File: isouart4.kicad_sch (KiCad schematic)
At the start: 25 parts, among them J1 USB_B, J2 Conn_01x04, J3 Conn_01x04, J4 Conn_01x04, J5 Conn_01x04, U1 AMS1117-3.3, U2 π122U31, U3 π122U31, U4 π122U31, U5 π122U31

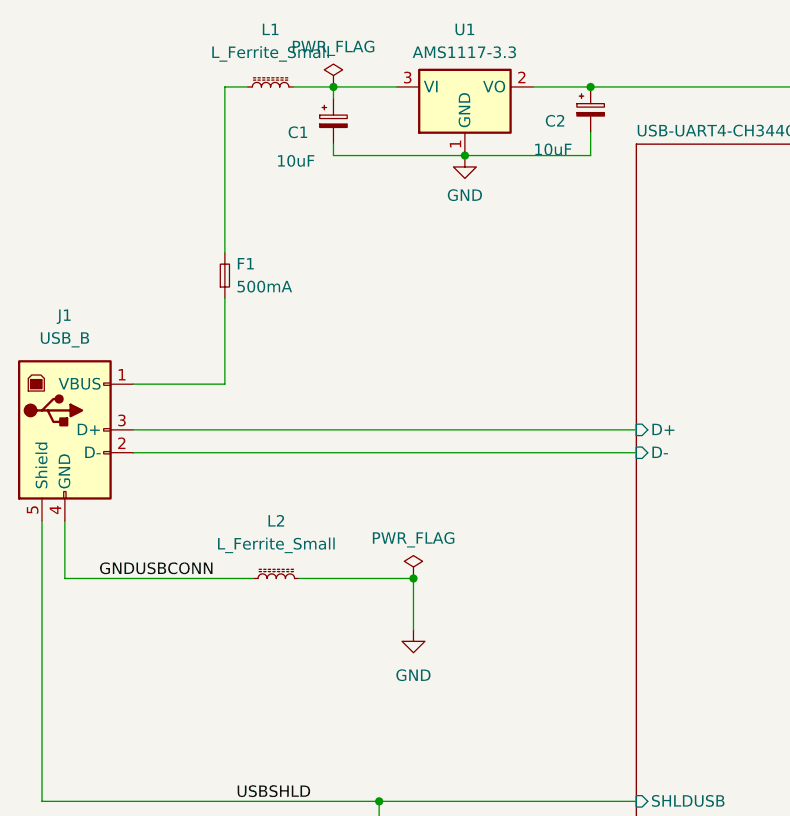
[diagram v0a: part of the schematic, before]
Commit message: adjust power filtering
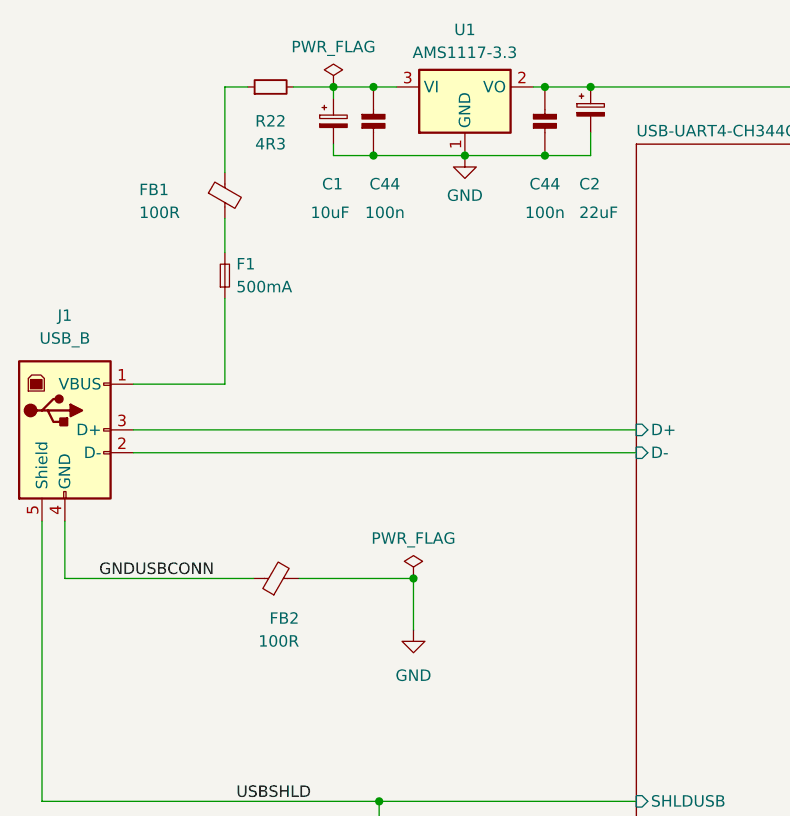
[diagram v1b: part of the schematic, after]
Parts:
- removed L1, L2: L_Ferrite_Small, isouart4:FB_0805_2012Metric, symbol isouart4:L_Ferrite_Small
- added C44 (x2): 100n, Capacitor_SMD:C_0805_2012Metric_Pad1.18x1.45mm_HandSolder, symbol isouart4:CAP_NP
- added FB1, FB2: 100R, isouart4:FB_0805_2012Metric, symbol Device:FerriteBead_Small
- added R22: 4R3, Resistor_SMD:R_2512_6332Metric_Pad1.40x3.35mm_HandSolder, symbol Device:R_Small
- C1: footprint Capacitor_SMD:C_0805_2012Metric_Pad1.18x1.45mm_HandSolder -> Capacitor_Tantalum_SMD:CP_EIA-3528-15_AVX-H_Pad1.50x2.35mm_HandSolder
- C2: value 10uF -> 22uF; footprint Capacitor_SMD:C_0805_2012Metric_Pad1.18x1.45mm_HandSolder -> Capacitor_Tantalum_SMD:CP_EIA-3528-15_AVX-H_Pad1.50x2.35mm_HandSolder
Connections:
- net GND: now also C44.2, C44.2, FB2.2
- net GNDUSBCONN: now also FB2.1
- net USB-UART4-CH344Q/VIN 3.3V: now also C44.1
- net at C1.1, U1.3 (VI): now also C44.1, R22.2
- net at F1.2: now also FB1.2
- new net: FB1.1, R22.1

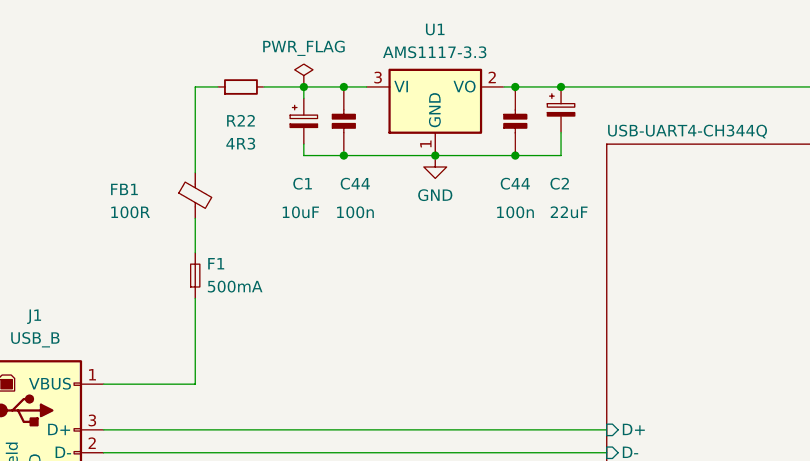
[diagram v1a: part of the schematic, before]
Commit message: AMS1117-3.3 -> LP2950CDT-3.3 (reduce usb downstream capacitance)
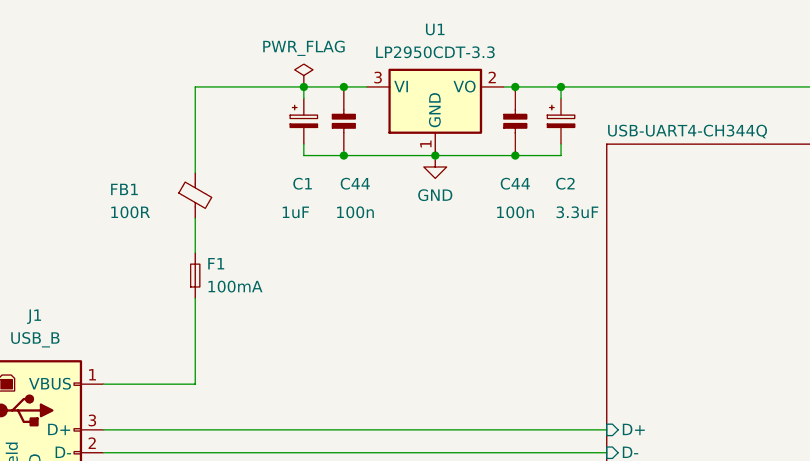
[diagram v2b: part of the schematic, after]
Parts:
- removed R22: 4R3, Resistor_SMD:R_2512_6332Metric_Pad1.40x3.35mm_HandSolder, symbol Device:R_Small
- C1: value 10uF -> 1uF
- C2: value 22uF -> 3.3uF
- F1: value 500mA -> 100mA
- U1: value AMS1117-3.3 -> LP2950CDT-3.3; footprint Package_TO_SOT_SMD:SOT-223-3_TabPin2 -> Package_TO_SOT_SMD:TO-252-2
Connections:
- net at C1.1, C44.1, U1.3 (VI): now also FB1.1
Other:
- moved on the sheet: C2
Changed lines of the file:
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@@
-    (stroke (width 0) (type default))
-  )
-  (wire (pts (xy 81.28 88.9) (xy 83.82 88.9))
     (stroke (width 0) (type default))
   )
@@
     (stroke (width 0) (type default))
   )
+  (wire (pts (xy 121.92 90.17) (xy 121.92 88.9))
+    (stroke (width 0) (type default))
+  )
   (wire (pts (xy 246.38 165.1) (xy 249.555 165.1))
     (stroke (width 0) (type default))
@@
     (stroke (width 0) (type default))
   )
-  (wire (pts (xy 121.92 93.98) (xy 121.92 96.52))
+  (wire (pts (xy 121.92 95.25) (xy 121.92 96.52))
     (stroke (width 0) (type default))
   )
@@
     (stroke (width 0) (type default))
   )
-  (wire (pts (xy 88.9 88.9) (xy 93.345 88.9))
+  (wire (pts (xy 81.28 88.9) (xy 93.345 88.9))
     (stroke (width 0) (type default))
   )
@@
       (effects (font (size 1.27 1.27)) (justify left))
     )
-    (property "Value" "10uF" (at 90.805 102.87 0)
+    (property "Value" "1uF" (at 90.805 102.87 0)
       (effects (font (size 1.27 1.27)) (justify left))
     )
@@
       (effects (font (size 1.27 1.27)) (justify right))
     )
-    (property "Value" "500mA" (at 82.55 111.125 90)
+    (property "Value" "100mA" (at 82.55 111.125 90)
       (effects (font (size 1.27 1.27)) (justify right))
     )
@@
         (path "/7c54d849-3d49-4f8e-b560-9dd1d738085c"
           (reference "#FLG02") (unit 1)
-        )
-      )
-    )
-  )
-  (symbol (lib_id "Device:R_Small") (at 86.36 88.9 90) (unit 1)
-    (in_bom yes) (on_board yes) (dnp no)
-    (property "Reference" "R22" (at 86.36 92.71 90)
-      (effects (font (size 1.27 1.27)))
-    )
-    (property "Value" "4R3" (at 86.36 95.25 90)
-      (effects (font (size 1.27 1.27)))
-    )
-    (property "Footprint" "Resistor_SMD:R_2512_6332Metric_Pad1.40x3.35mm_HandSolder" (at 86.36 88.9 0)
-      (effects (font (size 1.27 1.27)) hide)
-    )
-    (property "Datasheet" "~" (at 86.36 88.9 0)
-      (effects (font (size 1.27 1.27)) hide)
-    )
-    (pin "1")
-    (pin "2")
-    (instances
-      (project "4WD_UART"
-        (path "/3d727dd2-df65-4f49-bc46-de00aac75be7"
-          (reference "R22") (unit 1)
-        )
-      )
-      (project "isouart4"
-        (path "/7c54d849-3d49-4f8e-b560-9dd1d738085c/2d235b8c-e233-4472-a8af-47eb53407ee3"
-          (reference "R1") (unit 1)
-        )
-        (path "/7c54d849-3d49-4f8e-b560-9dd1d738085c"
-          (reference "R26") (unit 1)
         )
       )
@@
       (effects (font (size 1.27 1.27)))
     )
-    (property "Value" "AMS1117-3.3" (at 107.95 85.09 0)
-      (effects (font (size 1.27 1.27)))
-    )
-    (property "Footprint" "Package_TO_SOT_SMD:SOT-223-3_TabPin2" (at 107.95 83.82 0)
+    (property "Value" "LP2950CDT-3.3" (at 107.95 85.09 0)
+      (effects (font (size 1.27 1.27)))
+    )
+    (property "Footprint" "Package_TO_SOT_SMD:TO-252-2" (at 107.95 83.82 0)
       (effects (font (size 1.27 1.27)) hide)
     )
@@
     )
   )
-  (symbol (lib_id "Device:C_Polarized_Small") (at 121.92 91.44 0) (unit 1)
+  (symbol (lib_id "Device:C_Polarized_Small") (at 121.92 92.71 0) (unit 1)
     (in_bom yes) (on_board yes) (dnp no)
-    (property "Reference" "C2" (at 120.65 99.695 0)
-      (effects (font (size 1.27 1.27)) (justify left))
-    )
-    (property "Value" "22uF" (at 120.65 102.87 0)
-      (effects (font (size 1.27 1.27)) (justify left))
-    )
-    (property "Footprint" "Capacitor_Tantalum_SMD:CP_EIA-3528-15_AVX-H_Pad1.50x2.35mm_HandSolder" (at 121.92 91.44 0)
-      (effects (font (size 1.27 1.27)) hide)
-    )
-    (property "Datasheet" "~" (at 121.92 91.44 0)
-      (effects (font (size 1.27 1.27)) hide)
-    )
+    (property "Reference" "C2" (at 121.285 99.695 0)
+      (effects (font (size 1.27 1.27)) (justify left))
+    )
+    (property "Value" "3.3uF" (at 121.285 102.87 0)
+      (effects (font (size 1.27 1.27)) (justify left))
+    )
+    (property "Footprint" "Capacitor_Tantalum_SMD:CP_EIA-3528-15_AVX-H_Pad1.50x2.35mm_HandSolder" (at 121.92 92.71 0)
+      (effects (font (size 1.27 1.27)) hide)
+    )
+    (property "Datasheet" "~" (at 121.92 92.71 0)
+      (effects (font (size 1.27 1.27)) hide)
+    )

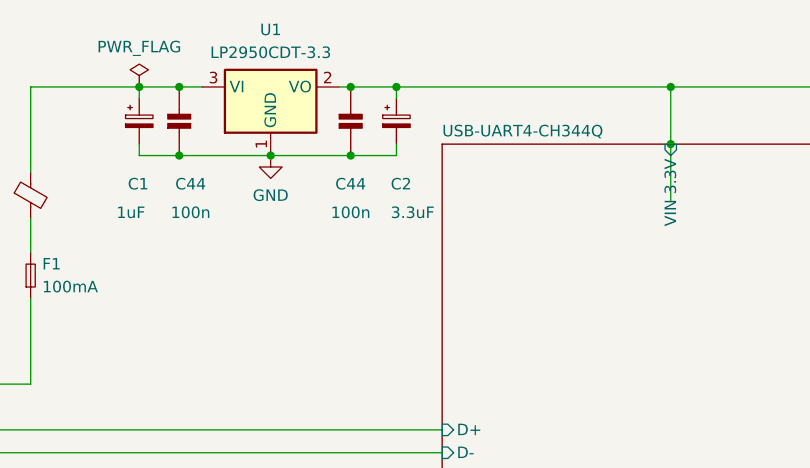
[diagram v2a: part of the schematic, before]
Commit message: adjust silkscreen and led positions; reannotate
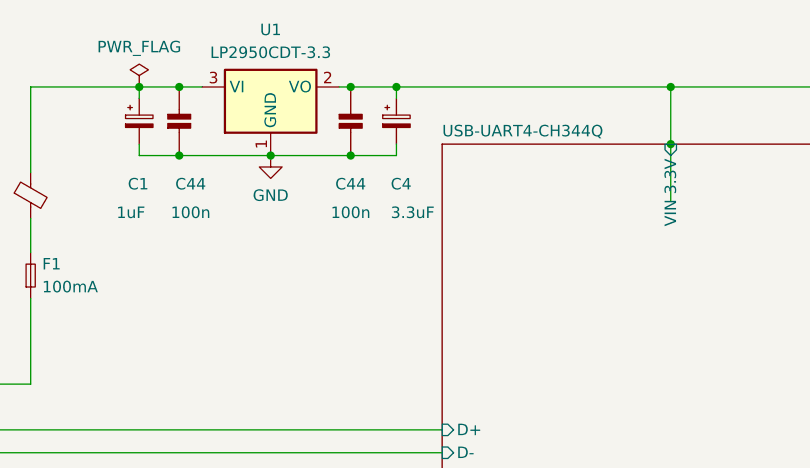
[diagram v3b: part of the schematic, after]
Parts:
- renumbered C2 to C4
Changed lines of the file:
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@@
         )
         (path "/7c54d849-3d49-4f8e-b560-9dd1d738085c"
-          (reference "C3") (unit 1)
+          (reference "C5") (unit 1)
         )
       )
@@
         )
         (path "/7c54d849-3d49-4f8e-b560-9dd1d738085c"
-          (reference "C30") (unit 1)
+          (reference "C2") (unit 1)
         )
       )
@@
         )
         (path "/7c54d849-3d49-4f8e-b560-9dd1d738085c"
-          (reference "C7") (unit 1)
+          (reference "C9") (unit 1)
         )
       )
@@
         )
         (path "/7c54d849-3d49-4f8e-b560-9dd1d738085c"
-          (reference "C5") (unit 1)
+          (reference "C7") (unit 1)
         )
       )
@@
         )
         (path "/7c54d849-3d49-4f8e-b560-9dd1d738085c"
-          (reference "C6") (unit 1)
+          (reference "C8") (unit 1)
         )
       )
@@
         )
         (path "/7c54d849-3d49-4f8e-b560-9dd1d738085c"
-          (reference "C31") (unit 1)
+          (reference "C3") (unit 1)
         )
       )
@@
   (symbol (lib_id "Device:C_Polarized_Small") (at 121.92 92.71 0) (unit 1)
     (in_bom yes) (on_board yes) (dnp no)
-    (property "Reference" "C2" (at 121.285 99.695 0)
+    (property "Reference" "C4" (at 121.285 99.695 0)
       (effects (font (size 1.27 1.27)) (justify left))
     )
@@
       (project "isouart4"
         (path "/7c54d849-3d49-4f8e-b560-9dd1d738085c"
-          (reference "C2") (unit 1)
+          (reference "C4") (unit 1)
         )
       )
@@
         )
         (path "/7c54d849-3d49-4f8e-b560-9dd1d738085c"
-          (reference "C4") (unit 1)
-        )
-      )
+          (reference "C6") (unit 1)
+        )
+      )

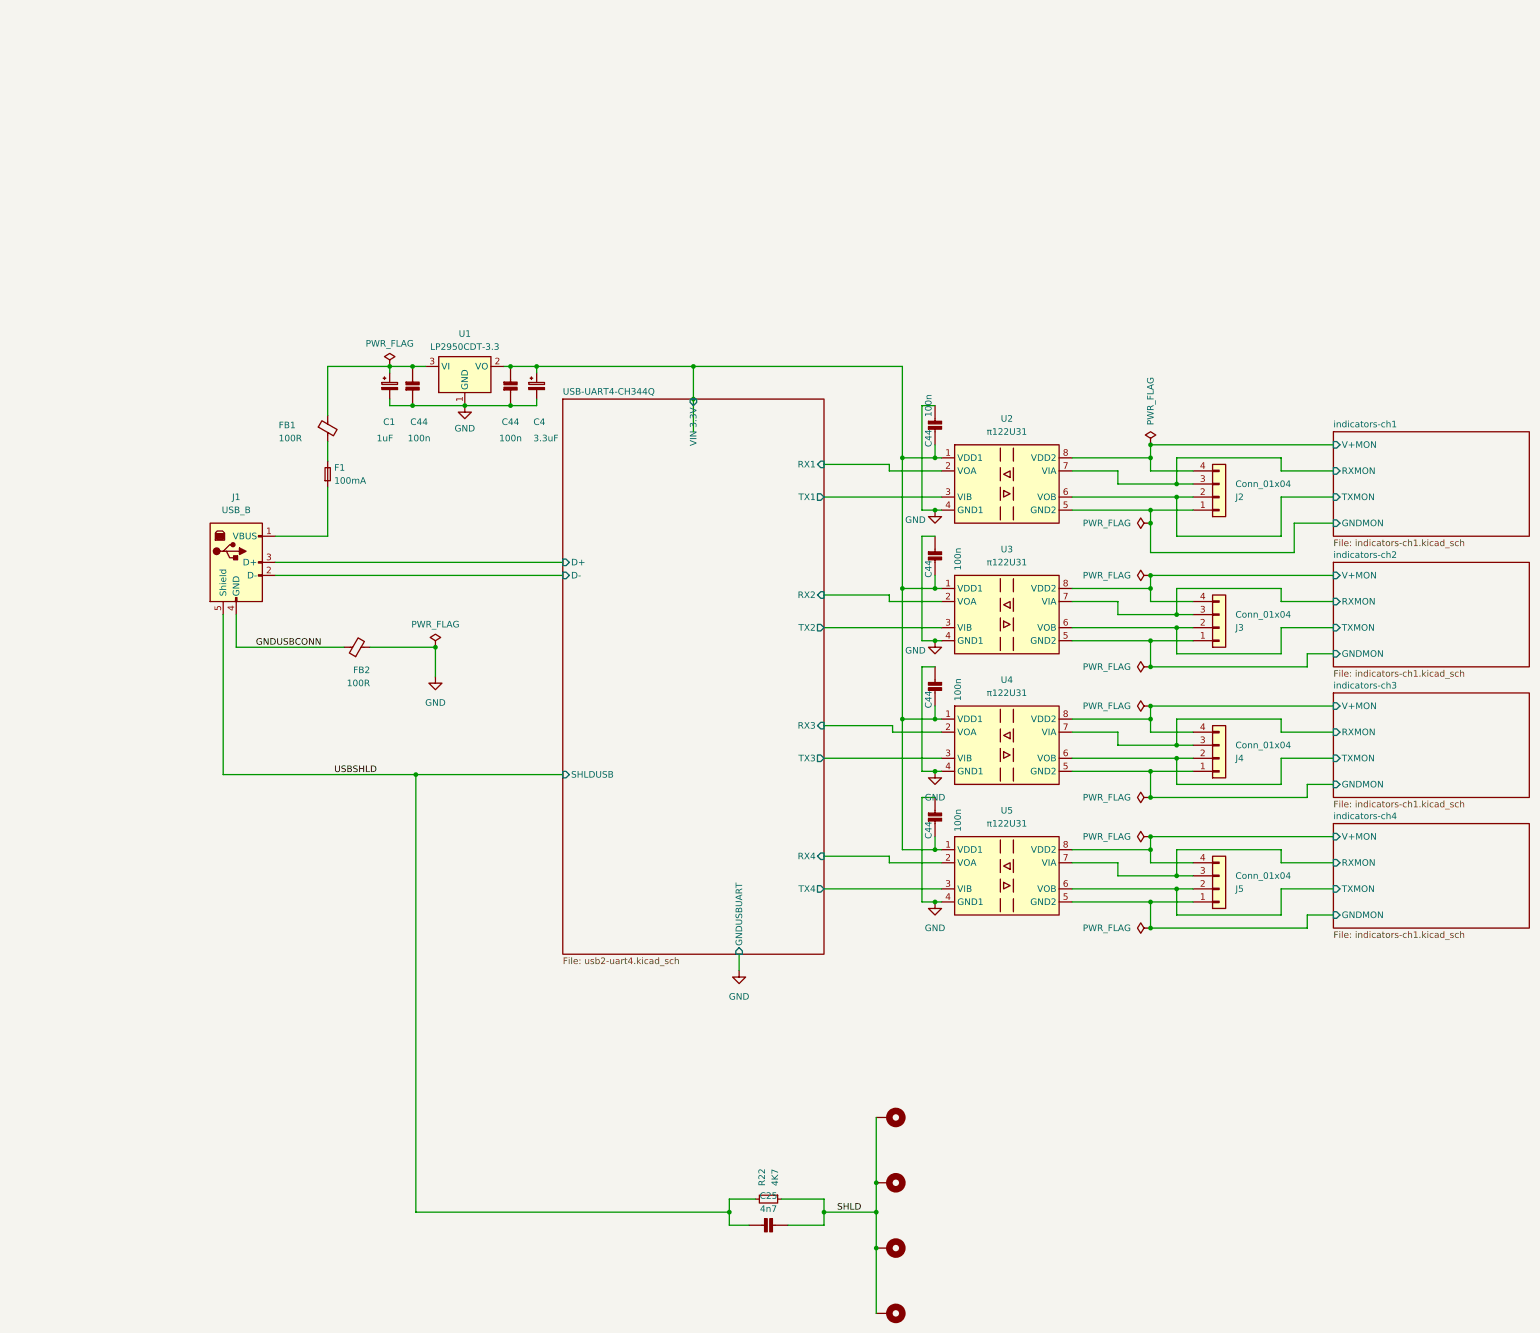
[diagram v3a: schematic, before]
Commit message: Switch main sheet of schematic from A3 to A4
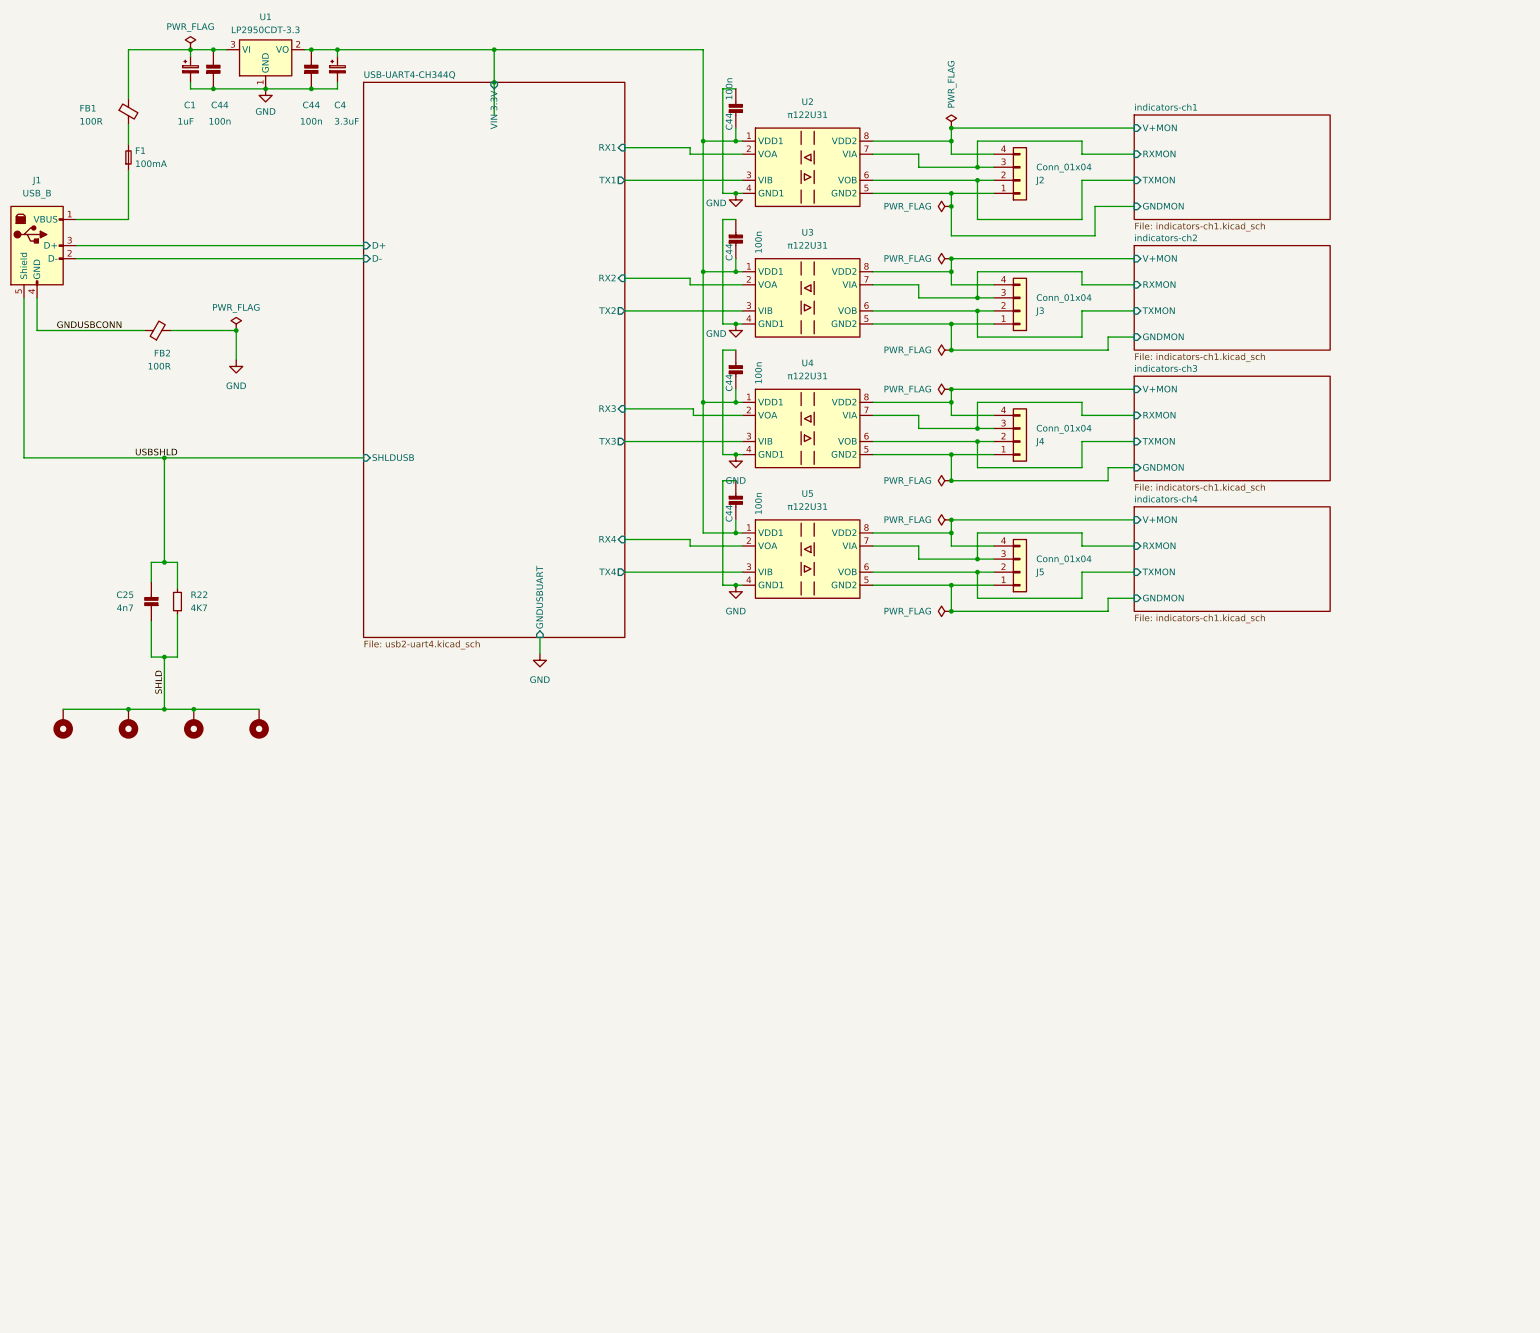
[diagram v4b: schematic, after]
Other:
- moved on the sheet: C1, C25, C4, C44, F1, FB1, FB2, J1, J2, J3, J4, J5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

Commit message: Add some title text to the schematic sheets
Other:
- note added: "Connectors, 3.3V regulator and isolators"
- title: (none) -> Galvanically Isolated USB attached Quad UART
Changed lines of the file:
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@@
 (kicad_sch (version 20230121) (generator eeschema)
   (paper "A4")
+  (title_block
+    (title "Galvanically Isolated USB attached Quad UART")
+  )
   (junction (at 160.655 106.045) (diameter 0) (color 0 0 0 0)
   )
@@
     (stroke (width 0) (type default))
   )
+  (text "Connectors, 3.3V regulator and isolators" (at 182.245 175.895 0)
+    (effects (font (size 3 3)) (justify left bottom))
+  )
   (label "USBSHLD" (at 43.815 106.68 0) (fields_autoplaced)
